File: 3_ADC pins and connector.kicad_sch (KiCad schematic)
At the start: 85 parts

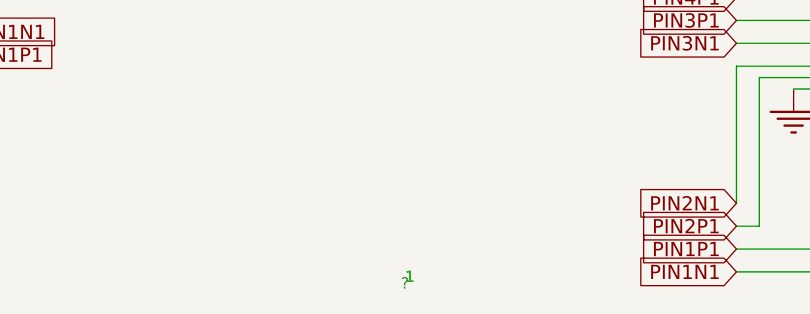
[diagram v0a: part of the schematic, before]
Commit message: Fix import2 ERC: pin types, references, and NC pins
- Convert EasyEDA R/C input pins to passive in lib_symbols and symbol library
- Set targeted pin types for ESP32-C6, TYPE-C, ADS1299 NC, TPD4E1B06, TPS62821
- Annotate Short-Symbol jumpers (JP1-6), sheet frames (F1-F2), and #PWR flags
- ERC: 576 violations / 122 errors -> 448 violations / 4 errors
- Net names unchanged; remaining errors are BIASIN/BIASOUT wiring and GND PWR_FLAG
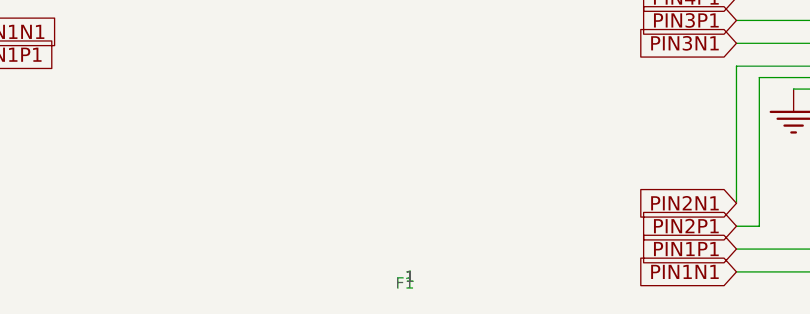
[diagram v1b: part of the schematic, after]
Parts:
- F1: renamed from ?; now left out of the parts list
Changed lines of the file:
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@@
 		(in_pos_files yes)
 		(dnp no)
-		(property "Reference" "#PWR?"
+		(property "Reference" "#PWR01"
 			(at 391.16 186.69 0)
 			(hide yes)
@@
 			(project "import2"
 				(path "/06cae45c-d474-473f-93a9-05a684cc4e1b/68715cd1-9dff-4f45-ad1f-26f03da81a9e"
-					(reference "#PWR?")
+					(reference "#PWR02")
 					(unit 1)
 				)
@@
 		(in_pos_files yes)
 		(dnp no)
-		(property "Reference" "#PWR?"
+		(property "Reference" "#PWR03"
 			(at 391.16 85.09 0)
 			(hide yes)
@@
 			(project "import2"
 				(path "/06cae45c-d474-473f-93a9-05a684cc4e1b/68715cd1-9dff-4f45-ad1f-26f03da81a9e"
-					(reference "#PWR?")
+					(reference "#PWR04")
 					(unit 1)
 				)
@@
 		(in_pos_files yes)
 		(dnp no)
-		(property "Reference" "#PWR?"
+		(property "Reference" "#PWR05"
 			(at 287.02 140.97 0)
 			(hide yes)
@@
 			(project "import2"
 				(path "/06cae45c-d474-473f-93a9-05a684cc4e1b/68715cd1-9dff-4f45-ad1f-26f03da81a9e"
-					(reference "#PWR?")
+					(reference "#PWR06")
 					(unit 1)
 				)
@@
 		(in_pos_files yes)
 		(dnp no)
-		(property "Reference" "#PWR?"
+		(property "Reference" "#PWR07"
 			(at 287.02 19.05 0)
 			(hide yes)
@@
 			(project "import2"
 				(path "/06cae45c-d474-473f-93a9-05a684cc4e1b/68715cd1-9dff-4f45-ad1f-26f03da81a9e"
-					(reference "#PWR?")
+					(reference "#PWR08")
 					(unit 1)
 				)
@@
 		(in_pos_files yes)
 		(dnp no)
-		(property "Reference" "#PWR?"
+		(property "Reference" "#PWR09"
 			(at 118.11 19.05 0)
 			(hide yes)
@@
 			(project "import2"
 				(path "/06cae45c-d474-473f-93a9-05a684cc4e1b/68715cd1-9dff-4f45-ad1f-26f03da81a9e"
-					(reference "#PWR?")
+					(reference "#PWR10")
 					(unit 1)
 				)
@@
 		(in_pos_files yes)
 		(dnp no)
-		(property "Reference" "#PWR?"
+		(property "Reference" "#PWR11"
 			(at 118.11 201.93 0)
 			(hide yes)
@@
 			(project "import2"
 				(path "/06cae45c-d474-473f-93a9-05a684cc4e1b/68715cd1-9dff-4f45-ad1f-26f03da81a9e"
-					(reference "#PWR?")
+					(reference "#PWR12")
 					(unit 1)
 				)
@@
 		(in_pos_files yes)
 		(dnp no)
-		(property "Reference" "#PWR?"
+		(property "Reference" "#PWR13"
 			(at 57.15 49.53 0)
 			(hide yes)
@@
 			(project "import2"
 				(path "/06cae45c-d474-473f-93a9-05a684cc4e1b/68715cd1-9dff-4f45-ad1f-26f03da81a9e"
-					(reference "#PWR?")
+					(reference "#PWR14")
 					(unit 1)
 				)
@@
 		(in_pos_files yes)
 		(dnp no)
-		(property "Reference" "#PWR?"
+		(property "Reference" "#PWR15"
 			(at 287.02 110.49 0)
 			(hide yes)
@@
 			(project "import2"
 				(path "/06cae45c-d474-473f-93a9-05a684cc4e1b/68715cd1-9dff-4f45-ad1f-26f03da81a9e"
-					(reference "#PWR?")
+					(reference "#PWR16")
 					(unit 1)
 				)
@@
 		(in_pos_files yes)
 		(dnp no)
-		(property "Reference" "#PWR?"
+		(property "Reference" "#PWR17"
 			(at 118.11 49.53 0)
 			(hide yes)
@@
 			(project "import2"
 				(path "/06cae45c-d474-473f-93a9-05a684cc4e1b/68715cd1-9dff-4f45-ad1f-26f03da81a9e"
-					(reference "#PWR?")
+					(reference "#PWR18")
 					(unit 1)
 				)
@@
 		(in_pos_files yes)
 		(dnp no)
-		(property "Reference" "#PWR?"
+		(property "Reference" "#PWR19"
 			(at 391.16 110.49 0)
 			(hide yes)
@@
 			(project "import2"
 				(path "/06cae45c-d474-473f-93a9-05a684cc4e1b/68715cd1-9dff-4f45-ad1f-26f03da81a9e"
-					(reference "#PWR?")
+					(reference "#PWR20")
 					(unit 1)
 				)
@@
 		(in_pos_files yes)
 		(dnp no)
-		(property "Reference" "#PWR?"
+		(property "Reference" "#PWR21"
 			(at 391.16 212.09 0)
 			(hide yes)
@@
 			(project "import2"
 				(path "/06cae45c-d474-473f-93a9-05a684cc4e1b/68715cd1-9dff-4f45-ad1f-26f03da81a9e"
-					(reference "#PWR?")
+					(reference "#PWR22")
 					(unit 1)
 				)
@@
 		(in_pos_files yes)
 		(dnp no)
-		(property "Reference" "#PWR?"
+		(property "Reference" "#PWR23"
 			(at 391.16 161.29 0)
 			(hide yes)
@@
 			(project "import2"
 				(path "/06cae45c-d474-473f-93a9-05a684cc4e1b/68715cd1-9dff-4f45-ad1f-26f03da81a9e"
-					(reference "#PWR?")
+					(reference "#PWR24")
 					(unit 1)
 				)
@@
 		(in_pos_files yes)
 		(dnp no)
-		(property "Reference" "#PWR?"
+		(property "Reference" "#PWR25"
 			(at 287.02 232.41 0)
 			(hide yes)
@@
 			(project "import2"
 				(path "/06cae45c-d474-473f-93a9-05a684cc4e1b/68715cd1-9dff-4f45-ad1f-26f03da81a9e"
-					(reference "#PWR?")
+					(reference "#PWR26")
 					(unit 1)
 				)
@@
 		(in_pos_files yes)
 		(dnp no)
-		(property "Reference" "#PWR?"
+		(property "Reference" "#PWR27"
 			(at 391.16 59.69 0)
 			(hide yes)
@@
 			(project "import2"
 				(path "/06cae45c-d474-473f-93a9-05a684cc4e1b/68715cd1-9dff-4f45-ad1f-26f03da81a9e"
-					(reference "#PWR?")
+					(reference "#PWR28")
 					(unit 1)
 				)
@@
 		(in_pos_files yes)
 		(dnp no)
-		(property "Reference" "#PWR?"
+		(property "Reference" "#PWR29"
 			(at 118.11 80.01 0)
 			(hide yes)
@@
 			(project "import2"
 				(path "/06cae45c-d474-473f-93a9-05a684cc4e1b/68715cd1-9dff-4f45-ad1f-26f03da81a9e"
-					(reference "#PWR?")
+					(reference "#PWR30")
 					(unit 1)
 				)
@@
 		(in_pos_files yes)
 		(dnp no)
-		(property "Reference" "#PWR?"
+		(property "Reference" "#PWR31"
 			(at 54.61 19.05 0)
 			(hide yes)
@@
 			(project "import2"
 				(path "/06cae45c-d474-473f-93a9-05a684cc4e1b/68715cd1-9dff-4f45-ad1f-26f03da81a9e"
-					(reference "#PWR?")
+					(reference "#PWR32")
 					(unit 1)
 				)
@@
 		(body_style 0)
 		(exclude_from_sim no)
-		(in_bom yes)
-		(on_board yes)
+		(in_bom no)
+		(on_board no)
 		(in_pos_files yes)
 		(dnp no)
-		(property "Reference" "?"
+		(property "Reference" "F1"
 			(at 347.98 259.08 0)
 			(show_name no)
@@
 			(project "import2"
 				(path "/06cae45c-d474-473f-93a9-05a684cc4e1b/68715cd1-9dff-4f45-ad1f-26f03da81a9e"
-					(reference "?")
+					(reference "F1")
 					(unit 0)
 				)
@@
 		(in_pos_files yes)
 		(dnp no)
-		(property "Reference" "#PWR?"
+		(property "Reference" "#PWR33"
 			(at 391.16 34.29 0)
 			(hide yes)
@@
 			(project "import2"
 				(path "/06cae45c-d474-473f-93a9-05a684cc4e1b/68715cd1-9dff-4f45-ad1f-26f03da81a9e"
-					(reference "#PWR?")
+					(reference "#PWR34")
 					(unit 1)
 				)
@@
 		(in_pos_files yes)
 		(dnp no)
-		(property "Reference" "#PWR?"
+		(property "Reference" "#PWR35"
 			(at 287.02 80.01 0)
 			(hide yes)
@@
 			(project "import2"
 				(path "/06cae45c-d474-473f-93a9-05a684cc4e1b/68715cd1-9dff-4f45-ad1f-26f03da81a9e"
-					(reference "#PWR?")
+					(reference "#PWR36")
 					(unit 1)
 				)
@@
 		(in_pos_files yes)
 		(dnp no)
-		(property "Reference" "#PWR?"
+		(property "Reference" "#PWR37"
 			(at 287.02 201.93 0)
 			(hide yes)
@@
 			(project "import2"
 				(path "/06cae45c-d474-473f-93a9-05a684cc4e1b/68715cd1-9dff-4f45-ad1f-26f03da81a9e"
-					(reference "#PWR?")
+					(reference "#PWR38")
 					(unit 1)
 				)
@@
 		(in_pos_files yes)
 		(dnp no)
-		(property "Reference" "#PWR?"
+		(property "Reference" "#PWR39"
 			(at 391.16 135.89 0)
 			(hide yes)
@@
 			(project "import2"
 				(path "/06cae45c-d474-473f-93a9-05a684cc4e1b/68715cd1-9dff-4f45-ad1f-26f03da81a9e"
-					(reference "#PWR?")
+					(reference "#PWR40")
 					(unit 1)
 				)
@@
 		(in_pos_files yes)
 		(dnp no)
-		(property "Reference" "#PWR?"
+		(property "Reference" "#PWR41"
 			(at 287.02 49.53 0)
 			(hide yes)
@@
 			(project "import2"
 				(path "/06cae45c-d474-473f-93a9-05a684cc4e1b/68715cd1-9dff-4f45-ad1f-26f03da81a9e"
-					(reference "#PWR?")
+					(reference "#PWR42")
 					(unit 1)
 				)
@@
 		(in_pos_files yes)
 		(dnp no)
-		(property "Reference" "#PWR?"
+		(property "Reference" "#PWR43"
 			(at 118.11 110.49 0)
 			(hide yes)
@@
 			(project "import2"
 				(path "/06cae45c-d474-473f-93a9-05a684cc4e1b/68715cd1-9dff-4f45-ad1f-26f03da81a9e"
-					(reference "#PWR?")
+					(reference "#PWR44")
 					(unit 1)
 				)
@@
 		(in_pos_files yes)
 		(dnp no)
-		(property "Reference" "#PWR?"
+		(property "Reference" "#PWR45"
 			(at 118.11 171.45 0)
 			(hide yes)
@@
 			(project "import2"
 				(path "/06cae45c-d474-473f-93a9-05a684cc4e1b/68715cd1-9dff-4f45-ad1f-26f03da81a9e"
-					(reference "#PWR?")
+					(reference "#PWR46")
 					(unit 1)
 				)
@@
 		(in_pos_files yes)
 		(dnp no)
-		(property "Reference" "#PWR?"
+		(property "Reference" "#PWR47"
 			(at 223.52 19.05 0)
 			(hide yes)
@@
 			(project "import2"
 				(path "/06cae45c-d474-473f-93a9-05a684cc4e1b/68715cd1-9dff-4f45-ad1f-26f03da81a9e"
-					(reference "#PWR?")
+					(reference "#PWR48")
 					(unit 1)
 				)
@@
 		(in_pos_files yes)
 		(dnp no)
-		(property "Reference" "#PWR?"
+		(property "Reference" "#PWR49"
 			(at 287.02 171.45 0)
 			(hide yes)
@@
 			(project "import2"
 				(path "/06cae45c-d474-473f-93a9-05a684cc4e1b/68715cd1-9dff-4f45-ad1f-26f03da81a9e"
-					(reference "#PWR?")
+					(reference "#PWR50")
 					(unit 1)
 				)
@@
 		(in_pos_files yes)
 		(dnp no)
-		(property "Reference" "#PWR?"
+		(property "Reference" "#PWR51"
 			(at 118.11 232.41 0)
 			(hide yes)
@@
 			(project "import2"
 				(path "/06cae45c-d474-473f-93a9-05a684cc4e1b/68715cd1-9dff-4f45-ad1f-26f03da81a9e"
-					(reference "#PWR?")
+					(reference "#PWR52")
 					(unit 1)
 				)
@@
 		(in_pos_files yes)
 		(dnp no)
-		(property "Reference" "#PWR?"
+		(property "Reference" "#PWR53"
 			(at 118.11 140.97 0)
 			(hide yes)
@@
 			(project "import2"
 				(path "/06cae45c-d474-473f-93a9-05a684cc4e1b/68715cd1-9dff-4f45-ad1f-26f03da81a9e"
-					(reference "#PWR?")
+					(reference "#PWR54")
 					(unit 1)
 				)
@@
 		(in_pos_files yes)
 		(dnp no)
-		(property "Reference" "#PWR?"
+		(property "Reference" "#PWR55"
 			(at 391.16 237.49 0)
 			(hide yes)
@@
 			(project "import2"
 				(path "/06cae45c-d474-473f-93a9-05a684cc4e1b/68715cd1-9dff-4f45-ad1f-26f03da81a9e"
-					(reference "#PWR?")
+					(reference "#PWR56")
 					(unit 1)
 				)

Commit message: Fix ERC
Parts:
- removed F1: (no value), ProPrj_BCI-easyedapro:, symbol ProPrj_BCI-easyedapro:Sheet-Symbol_A4
